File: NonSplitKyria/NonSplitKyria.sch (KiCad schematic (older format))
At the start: 104 parts, among them J1 USB2_C_Receptacle, SW1 Reset, U1 ATmega32U4-AU, Y1 16MHz

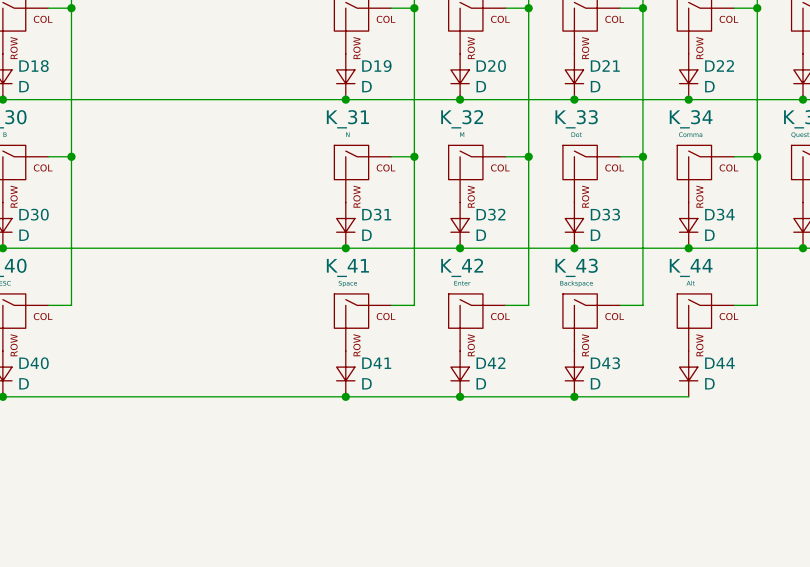
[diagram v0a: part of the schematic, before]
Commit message: Route Diodes
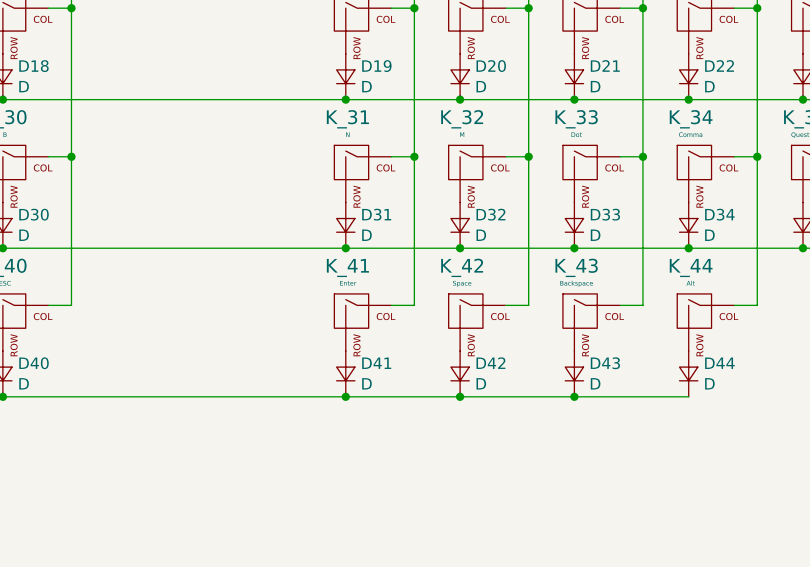
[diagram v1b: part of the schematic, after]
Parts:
- renumbered K_42 to K_41, K_41 to K_42
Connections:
- net col6: now also K_41.1 (COL); no longer K_42.1 (COL)
- net col7: now also K_42.1 (COL); no longer K_41.1 (COL)
- net at K_42.2 (ROW): now also D42.2 (A); no longer D41.2 (A)
- net at K_41.2 (ROW): now also D41.2 (A); no longer D42.2 (A)
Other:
- moved on the sheet: K_41, K_42
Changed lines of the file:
@@
 Connection ~ 10425 3400
 Connection ~ 10925 3400
-Connection ~ 12925 3400
 Connection ~ 13925 3400
 Connection ~ 9225 1700
@@
 Connection ~ 1200 3900
 Connection ~ 11425 3400
-Connection ~ 13425 3400
 Connection ~ 11725 2350
 Connection ~ 13725 2350
@@
 Connection ~ 11425 2750
 Connection ~ 12925 2750
+Connection ~ 12925 3400
+Connection ~ 13425 3400
 NoConn ~ 2150 2550
 Wire Wire Line
@@
 $EndComp
 $Comp
-L power:+5V #PWR?
+L power:+5V #PWR011
 U 1 1 5EEFF72F
 P 1200 3775
-F 0 "#PWR?" H 1200 3625 50  0001 C CNN
+F 0 "#PWR011" H 1200 3625 50  0001 C CNN
 F 1 "+5V" H 1215 3945 50  0000 C CNN
 F 2 "" H 1200 3775 50  0001 C CNN
@@
 $Comp
 L keyboard-cache:MX_Alps_Hybrid_MX-NoLED K_41
-U 1 1 5EE39E91
+U 1 1 5EE39F12
 P 12975 3050
 F 0 "K_41" H 12934 3271 60  0000 C CNN
-F 1 "Space" H 12934 3196 20  0000 C CNN
+F 1 "Enter" H 12934 3196 20  0000 C CNN
 F 2 "MX_Only:MXOnly-1U-NoLED" H 12350 3025 60  0001 C CNN
 F 3 "" H 12350 3025 60  0001 C CNN
@@
 $Comp
 L keyboard-cache:MX_Alps_Hybrid_MX-NoLED K_42
-U 1 1 5EE39F12
+U 1 1 5EE39E91
 P 13475 3050
 F 0 "K_42" H 13434 3271 60  0000 C CNN
-F 1 "Enter" H 13434 3196 20  0000 C CNN
+F 1 "Space" H 13434 3196 20  0000 C CNN
 F 2 "MX_Only:MXOnly-1U-NoLED" H 12850 3025 60  0001 C CNN
 F 3 "" H 12850 3025 60  0001 C CNN

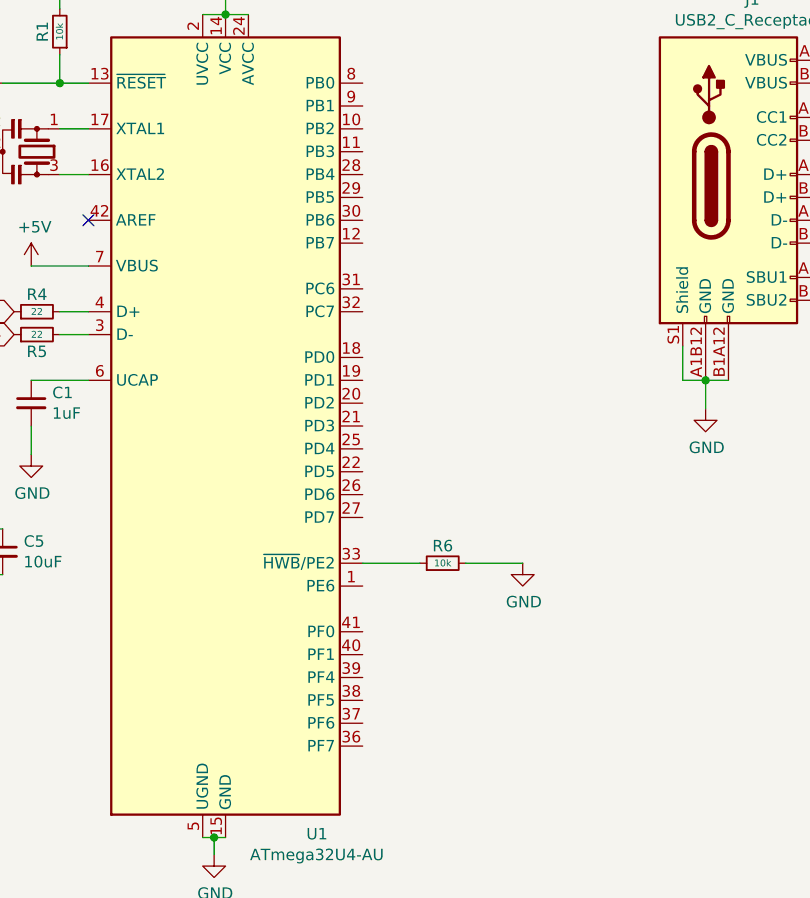
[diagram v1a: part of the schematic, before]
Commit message: Route MCU rows + cols
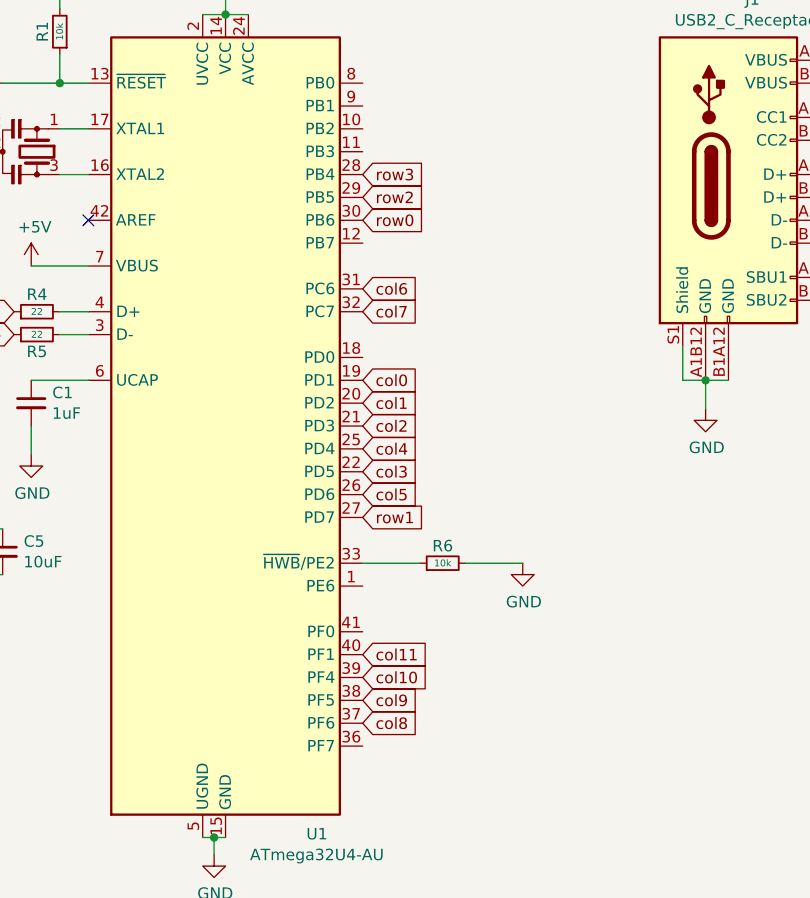
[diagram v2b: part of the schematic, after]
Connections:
- net col0: now also U1.19 (PD1)
- net col1: now also U1.20 (PD2)
- net col10: now also U1.39 (PF4)
- net col11: now also U1.40 (PF1)
- net col2: now also U1.21 (PD3)
- net col3: now also U1.22 (PD5)
- net col4: now also U1.25 (PD4)
- net col5: now also U1.26 (PD6)
- net col6: now also U1.31 (PC6)
- net col7: now also U1.32 (PC7)
- net col8: now also U1.37 (PF6)
- net col9: now also U1.38 (PF5)
- net row0: now also U1.30 (PB6)
- net row1: now also U1.27 (PD7)
- net row2: now also U1.29 (PB5)
- net row3: now also U1.28 (PB4)
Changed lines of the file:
@@
 Text GLabel 1825 3050 0    50   Input ~ 0
 D-
+Text GLabel 3350 2350 2    50   Input ~ 0
+row3
+Text GLabel 3350 2450 2    50   Input ~ 0
+row2
+Text GLabel 3350 2550 2    50   Input ~ 0
+row0
+Text GLabel 3350 2850 2    50   Input ~ 0
+col6
+Text GLabel 3350 2950 2    50   Input ~ 0
+col7
+Text GLabel 3350 3250 2    50   Input ~ 0
+col0
+Text GLabel 3350 3350 2    50   Input ~ 0
+col1
+Text GLabel 3350 3450 2    50   Input ~ 0
+col2
+Text GLabel 3350 3550 2    50   Input ~ 0
+col4
+Text GLabel 3350 3650 2    50   Input ~ 0
+col3
+Text GLabel 3350 3750 2    50   Input ~ 0
+col5
+Text GLabel 3350 3850 2    50   Input ~ 0
+row1
+Text GLabel 3350 4450 2    50   Input ~ 0
+col11
+Text GLabel 3350 4550 2    50   Input ~ 0
+col10
+Text GLabel 3350 4650 2    50   Input ~ 0
+col9
+Text GLabel 3350 4750 2    50   Input ~ 0
+col8
 Text GLabel 5725 2400 2    50   Input ~ 0
 D+
